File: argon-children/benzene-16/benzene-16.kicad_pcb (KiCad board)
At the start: 2 copper layers, 25 x 25 mm, 19 parts, among them U1 Conn1, U3 Conn2, U4 LMC555, U5 IS25WP256D-xM

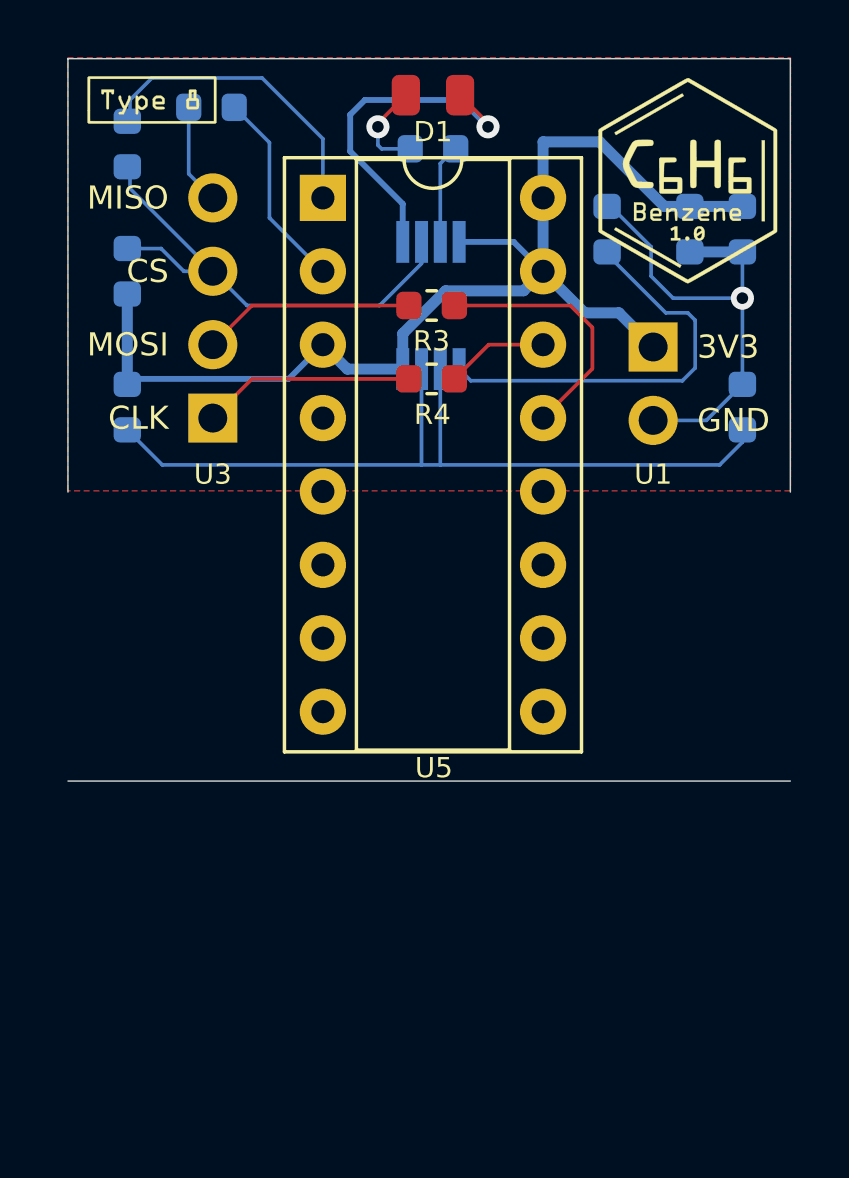
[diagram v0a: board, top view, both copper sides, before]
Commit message: Argon USB & custom footprint for DIP-16
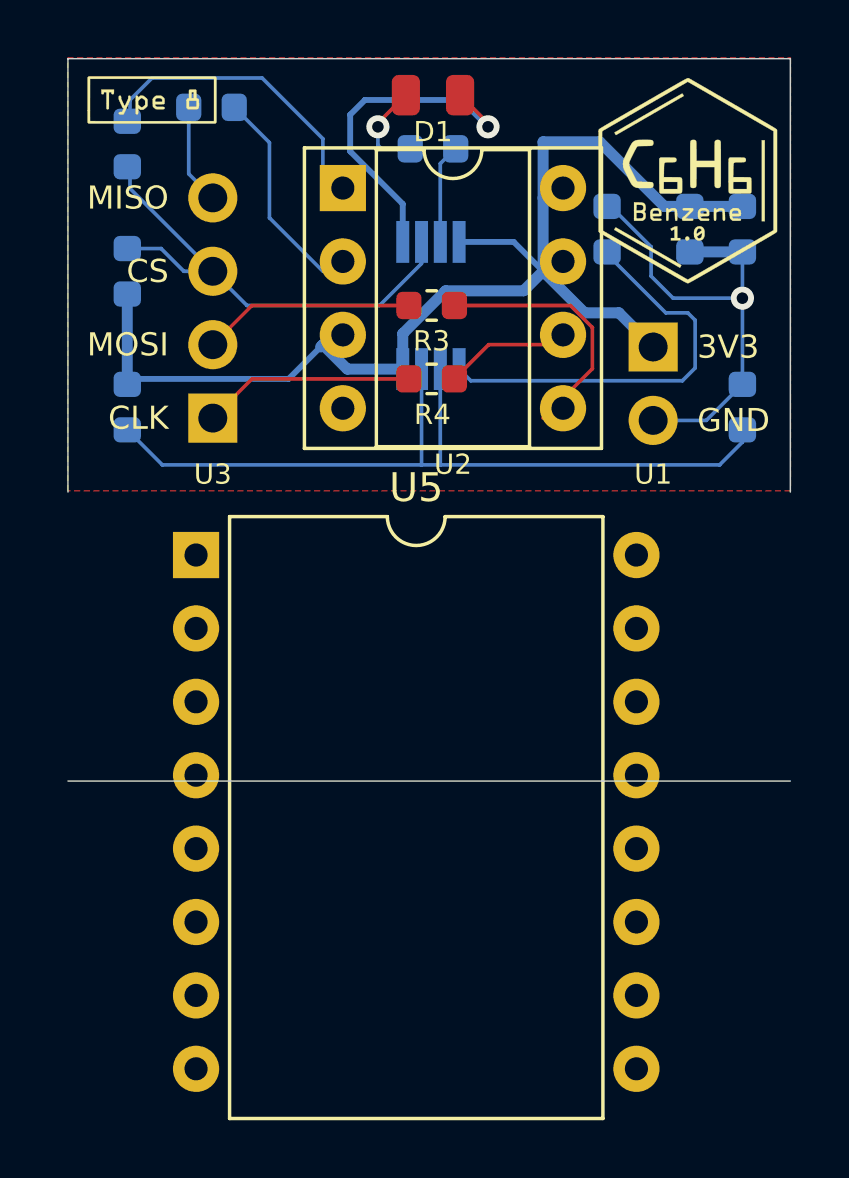
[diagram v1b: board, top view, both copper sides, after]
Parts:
- added U2: SPI FLASH, benzene:DIP-8_W7.62mm_Socket, F.Cu at (100.5, 72.5)
- U5: footprint Package_DIP:DIP-16_W7.62mm_Socket -> benzene:DIP-16_W15.24mm
- moved U5 13.1 mm to (95.4, 85.2)

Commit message: Aegon USB and power
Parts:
- added U1: Conn1, Connector_PinHeader_2.54mm:PinHeader_1x02_P2.54mm_Vertical, B.Cu at (102.2, 83.9)
- added U3: Conn2, Connector_PinHeader_2.54mm:PinHeader_1x04_P2.54mm_Vertical, B.Cu at (107.3, 95.5)
- moved U5 12.6 mm to (95.9, 72.6)
- moved U3 6.28 mm to (89.7, 80.4)
- moved U1 5.08 mm to (116.3, 78.0)
- moved G*** 2.71 mm to (115.1, 71.8)
- moved U2 0.82 mm to (99.7, 72.6)
- moved D1 0.12 mm to (103.5, 69.3)
- moved R6 0.12 mm to (103.5, 71.1)
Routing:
- net V3V3: track 42.0 -> 0.00 mm
- net Net-(C4-Pad1): track 29.2 -> 0.00 mm
- net GND: track 28.8 -> 0.00 mm, vias 2 -> 0
- net ~CS: track 17.2 -> 0.00 mm
- net Net-(C3-Pad1): track 14.2 -> 0.00 mm
- net Net-(R2-Pad1): track 10.6 -> 0.00 mm
- net Net-(R3-Pad1): track 8.93 -> 0.00 mm
- net Net-(R4-Pad2): track 7.35 -> 0.00 mm
- net Net-(R3-Pad2): track 7.35 -> 0.00 mm
- net Net-(R1-Pad1): track 6.94 -> 0.00 mm
- net Net-(R4-Pad1): track 3.56 -> 0.00 mm
- net Net-(R1-Pad2): track 3.48 -> 0.00 mm
- net Net-(R6-Pad1): track 3.46 -> 0.00 mm
- net Net-(D1-Pad2): track 3.30 -> 0.00 mm, vias 1 -> 0
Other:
- board size 25 x 25 mm -> 30 x 30 mm

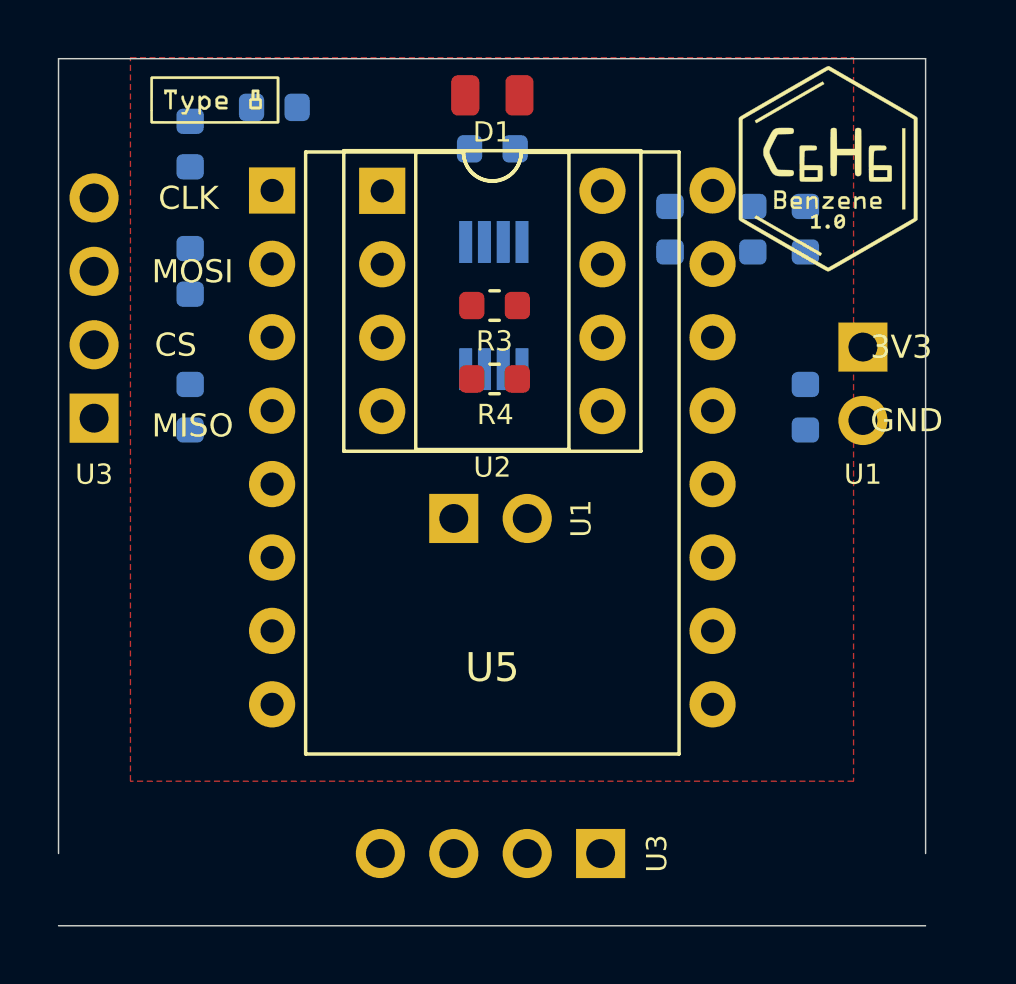
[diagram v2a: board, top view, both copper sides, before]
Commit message: 10.16mm between sockets on argon & benzene
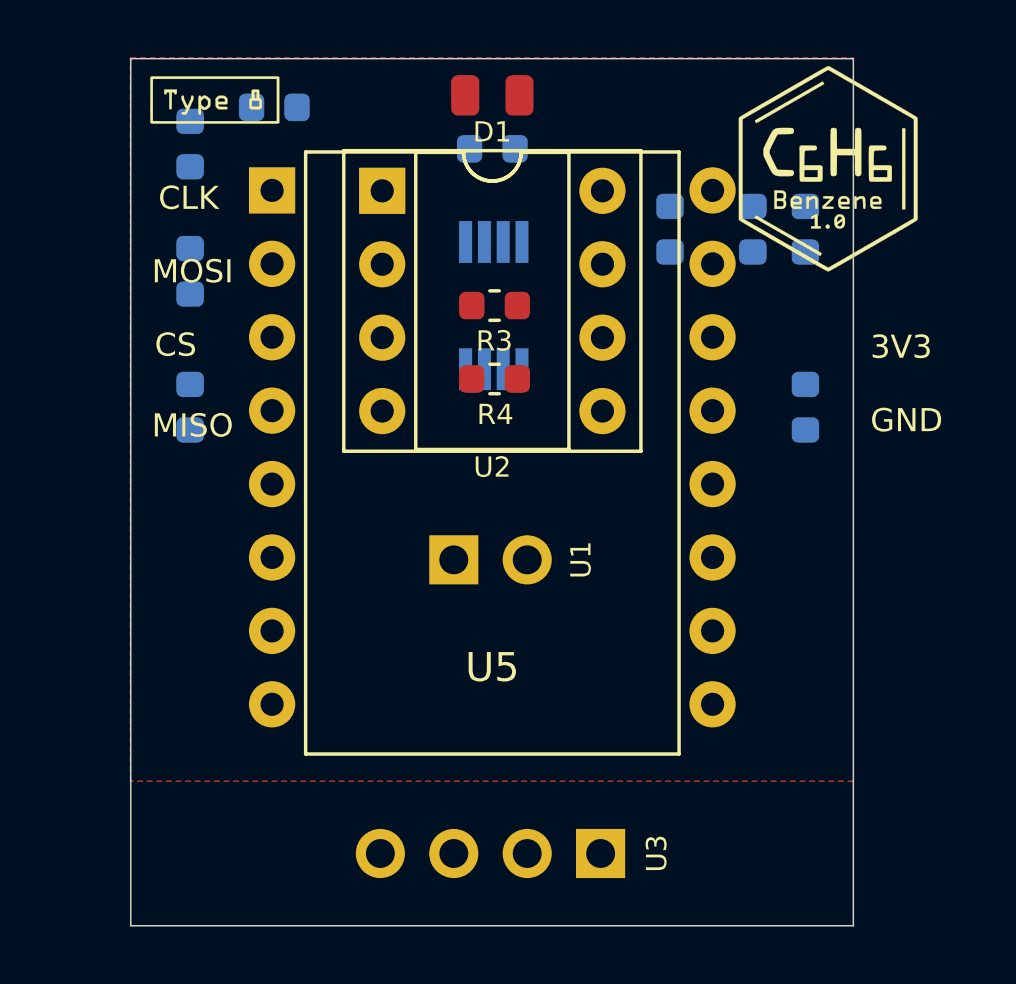
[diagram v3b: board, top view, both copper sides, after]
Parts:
- removed the U1 at (116.3, 78.0)
- removed the U3 at (89.7, 80.4)
- moved U1 1.43 mm to (102.2, 85.3)
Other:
- board size 30 x 30 mm -> 25 x 30 mm

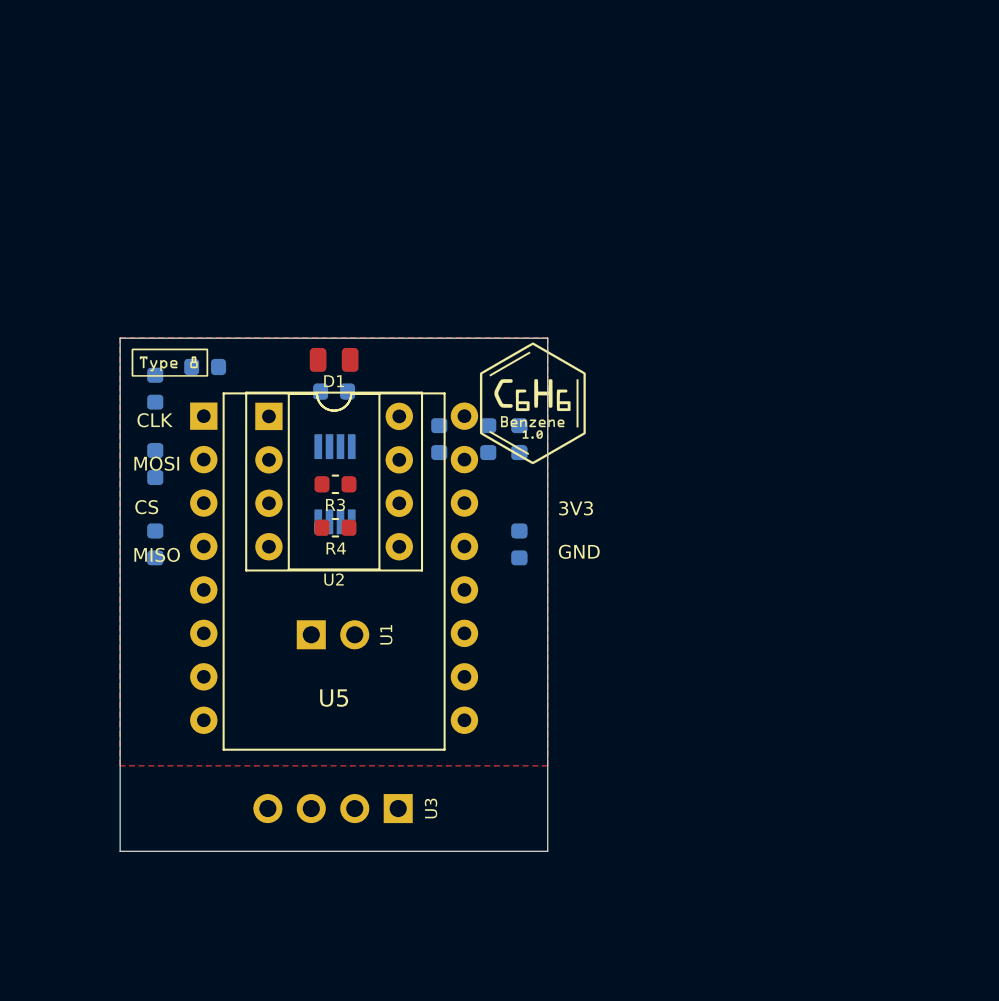
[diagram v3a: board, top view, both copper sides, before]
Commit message: Argon & beznen compatible
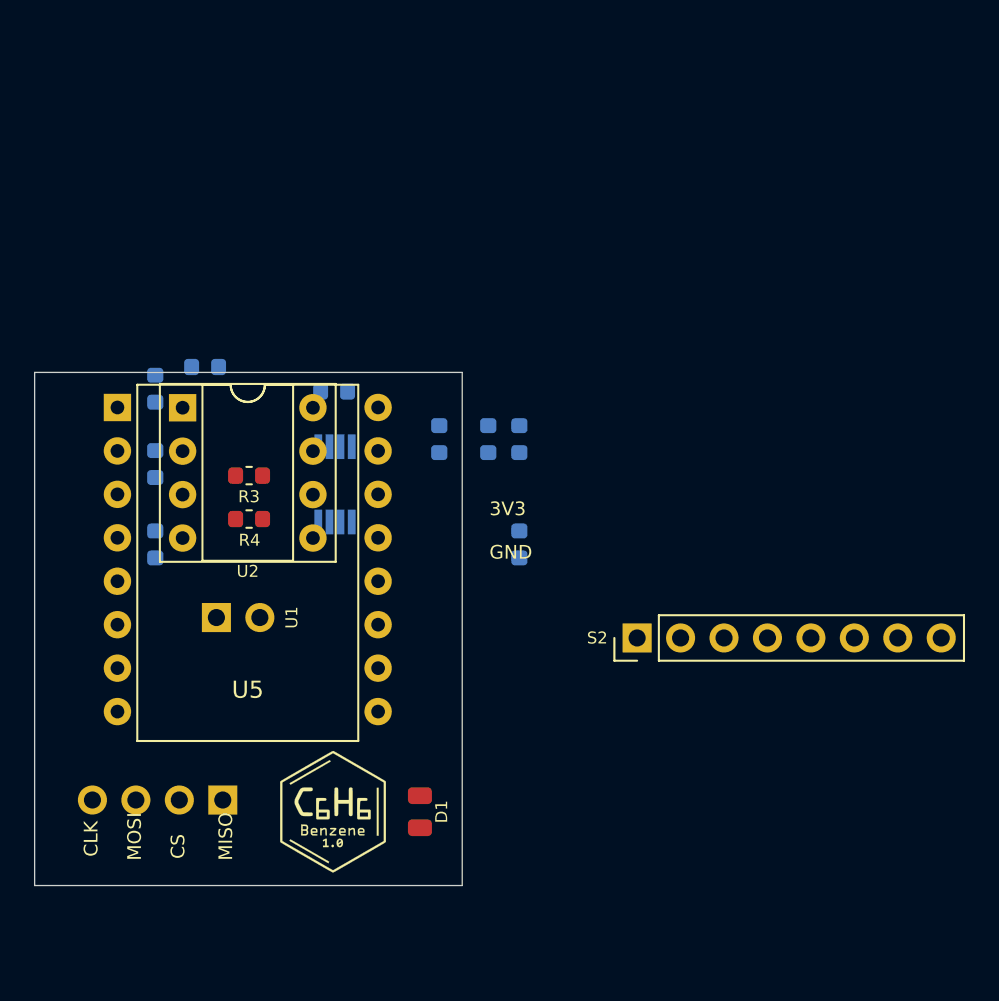
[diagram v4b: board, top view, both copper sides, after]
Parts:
- removed the G*** at (93.9, 69.4)
- added S2: Connector8, Connector_PinHeader_2.54mm:PinHeader_1x08_P2.54mm_Vertical, F.Cu at (121.2, 85.5)
- moved D1 26.9 mm to (108.5, 95.7), turned to 270 degrees
- moved G*** 26.6 mm to (103.4, 95.7)
- moved U3 10.3 mm to (97.0, 95.0)
- moved U1 5.64 mm to (96.6, 84.3)
- moved R4 5.07 mm to (98.5, 78.6)
- moved U2 5.07 mm to (94.7, 72.1)
- moved U5 5.07 mm to (90.8, 72.0)
- moved R3 5.07 mm to (98.5, 76.0)
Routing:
- removed copper zone on F.Cu, net GND

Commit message: Benzene pcb
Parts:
- removed G***: LOGO, benzene:author
- removed G***: LOGO, benzene:logo-wlasciwe
- removed the R1 at (96.0, 69.7)
- removed S2: Connector8, Connector_PinHeader_2.54mm:PinHeader_1x08_P2.54mm_Vertical
- removed the U2 at (94.7, 72.1)
- removed U5: IS25WP256D-xM, benzene:DIP-16_W15.24mm
- added C5: 10uF, Capacitor_Tantalum_SMD:CP_EIA-3216-18_Kemet-A, F.Cu at (108.2, 77.3)
- added C6: 100nF, Capacitor_SMD:C_0603_1608Metric, F.Cu at (102.7, 81.4)
- added J1: Conn2, Connector_PinHeader_2.54mm:PinHeader_1x04_P2.54mm_Vertical, F.Cu at (89.5, 93.7)
- added J2: Conn1, Connector_PinHeader_2.54mm:PinHeader_1x02_P2.54mm_Vertical, F.Cu at (97.1, 83.5)
- added R5: 47R, Resistor_SMD:R_0603_1608Metric, F.Cu at (107.3, 80.1)
- C1: value 100nF -> 10uF; footprint Capacitor_SMD:C_0603_1608Metric -> Capacitor_Tantalum_SMD:CP_EIA-3216-18_Kemet-A; moved to F.Cu
- C2: value 10uF -> 100nF; moved to F.Cu
- C3: value 10uF -> 10nF
- C4: value 1uF -> 100nF
- R2: moved to F.Cu
- R6: renamed from R7; value 100K -> 1M
- U1: value Conn1 -> DIP-8; footprint Connector_PinHeader_2.54mm:PinHeader_1x02_P2.54mm_Vertical -> benzene:DIP-8_W7.62mm_Socket; moved to F.Cu
- U3: value Conn2 -> DIP-16; footprint Connector_PinHeader_2.54mm:PinHeader_1x04_P2.54mm_Vertical -> benzene:DIP-16_W15.24mm; moved to F.Cu
- moved R2 26.8 mm to (119.1, 64.5), turned to 0 degrees
- moved U3 23.8 mm to (90.9, 72.0), turned to 0 degrees
- moved R4 23.6 mm to (119.1, 67.0), turned to 0 degrees
- moved R3 16.2 mm to (114.7, 76.5), turned to 0 degrees
- moved C2 12.8 mm to (119.1, 62.0), turned to 0 degrees
- moved U1 12.5 mm to (94.7, 72.0), turned to 0 degrees
- moved C1 4.36 mm to (108.2, 74.1), turned to 0 degrees
- renumbered R5 to R1, R6 to R7, U4 to U2
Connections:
- C2 pad 1: V3V3 -> GND
- C2 pad 2: GND -> V3V3
- C3 pad 1: Net-(C3-Pad1) -> GND
- C3 pad 2: GND -> Net-(C3-Pad2)
- R1 pad 1: ~CS -> V3V3
- R1 pad 2: V3V3 -> CS
- R2 pad 1: Net-(R2-Pad1) -> CS
- R2 pad 2: ~CS -> Net-(J1-Pad4)
- R3 pad 1: Net-(R3-Pad1) -> MISO
- R4 pad 1: Net-(R4-Pad1) -> MOSI
- U1 pad 1: (no net) -> CS
- U1 pad 2: (no net) -> MISO
- U2 pad 2: ~CS -> (no net)
- U2 pad 5: Net-(C3-Pad1) -> Net-(C3-Pad2)
- U3 pad 2: (no net) -> V3V3
- U3 pad 3: (no net) -> V3V3
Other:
- board text added: "SCK"
- board text removed: "CLK"

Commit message: Benzene PCB
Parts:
- added G***: LOGO, benzene:benzene-duze, F.Cu at (116.0, 75.8)
- C1, C5: footprint Capacitor_Tantalum_SMD:CP_EIA-3216-18_Kemet-A -> argon:CP_EIA-3216-18_Kemet-A; moved to B.Cu
- C2, C6, R2, R3, R4, R5: moved to B.Cu
- U1: footprint benzene:DIP-8_W7.62mm_Socket -> benzene:DIP-8_W7.62mm_Socket_wihtout_lines
- U3: footprint benzene:DIP-16_W15.24mm -> benzene:DIP-16_W15.24mm_without_lines
- moved C5 26.2 mm to (97.2, 53.5), turned to 90 degrees
- moved R6 23.8 mm to (116.0, 73.9), turned to 180 degrees
- moved C6 23.5 mm to (97.2, 58.5), turned to 90 degrees
- moved C1 21.9 mm to (107.8, 52.3), turned to 180 degrees
- moved D1 21.8 mm to (110.3, 73.9), turned to 180 degrees
- moved U1 21.8 mm to (103.9, 52.3)
- moved U3 21.8 mm to (100.1, 52.3)
- moved J1 21.8 mm to (98.7, 73.9)
- moved J2 21.8 mm to (106.4, 63.8)
- moved R4 20.5 mm to (101.3, 77.2), turned to 90 degrees
- moved R2 18.0 mm to (106.4, 77.2), turned to 90 degrees
- moved C2 13.2 mm to (107.8, 55.1)
- moved R1 11.1 mm to (103.2, 70.9), turned to 90 degrees
- moved R3 10.9 mm to (103.8, 77.2), turned to 90 degrees
- moved C3 10.3 mm to (112.2, 63.9), turned to 270 degrees
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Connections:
- U2 pad 2: (no net) -> CS
- U3 pad 1: (no net) -> V3V3
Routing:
- net V3V3: track 0.00 -> 74.6 mm, vias 0 -> 4
- net GND: track 0.00 -> 43.2 mm, vias 0 -> 4
- net SCK: track 0.00 -> 41.3 mm, vias 0 -> 1
- net CS: track 0.00 -> 37.9 mm
- net MOSI: track 0.00 -> 37.7 mm, vias 0 -> 1
- net MISO: track 0.00 -> 36.7 mm, vias 0 -> 2
- net Net-(D1-Pad2): track 0.00 -> 20.5 mm, vias 0 -> 1
- net Net-(C4-Pad1): track 0.00 -> 15.1 mm
- net Net-(R7-Pad1): track 0.00 -> 5.34 mm
- net Net-(C3-Pad2): track 0.00 -> 4.99 mm
- net Net-(J1-Pad3): track 0.00 -> 2.51 mm
- net Net-(J1-Pad2): track 0.00 -> 2.51 mm
- net Net-(J1-Pad1): track 0.00 -> 2.51 mm
- net Net-(J1-Pad4): track 0.00 -> 2.48 mm
- added copper zone on B.Cu, net GND
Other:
- net class Default: clearance 0.127 -> 0.1524
- net class zasilanie: clearance 0.381 -> 0.1524
- rule trace_clearance: 0.127 -> 0.1524

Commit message: Fix benzene bug (gnd & 3v3)
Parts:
- moved J2 2.54 mm to (108.9, 63.8), turned to 270 degrees
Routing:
- net GND: track 43.2 -> 49.9 mm
- net V3V3: track 74.6 -> 80.6 mm
